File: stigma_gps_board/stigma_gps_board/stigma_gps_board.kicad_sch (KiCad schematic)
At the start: 7 parts, among them J2 Conn_02x05_Counter_Clockwise, U2 SAM-M10Q

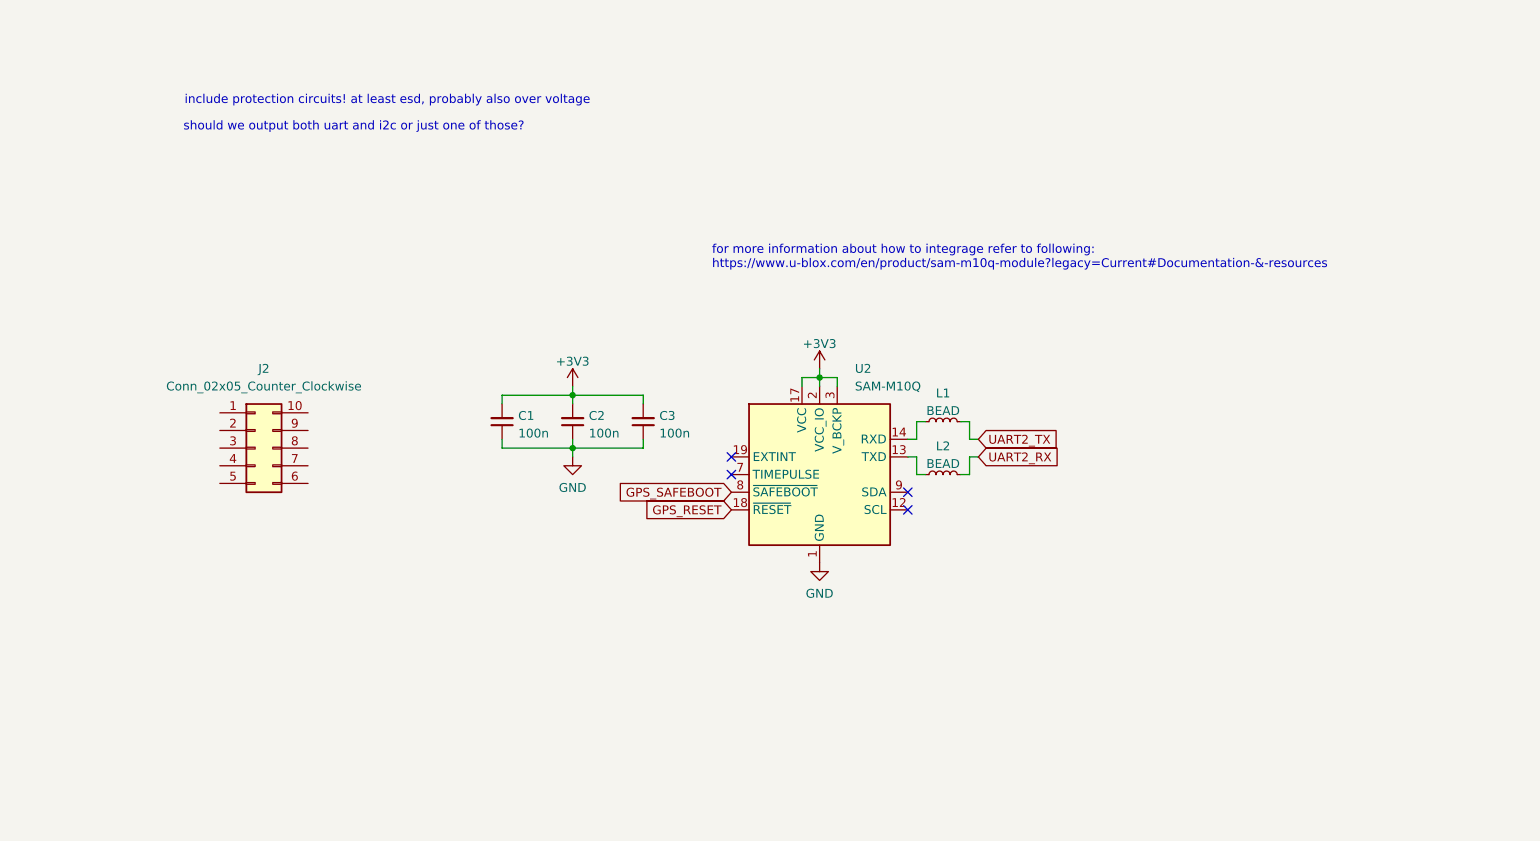
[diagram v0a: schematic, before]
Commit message: added esd protection, finished scematic
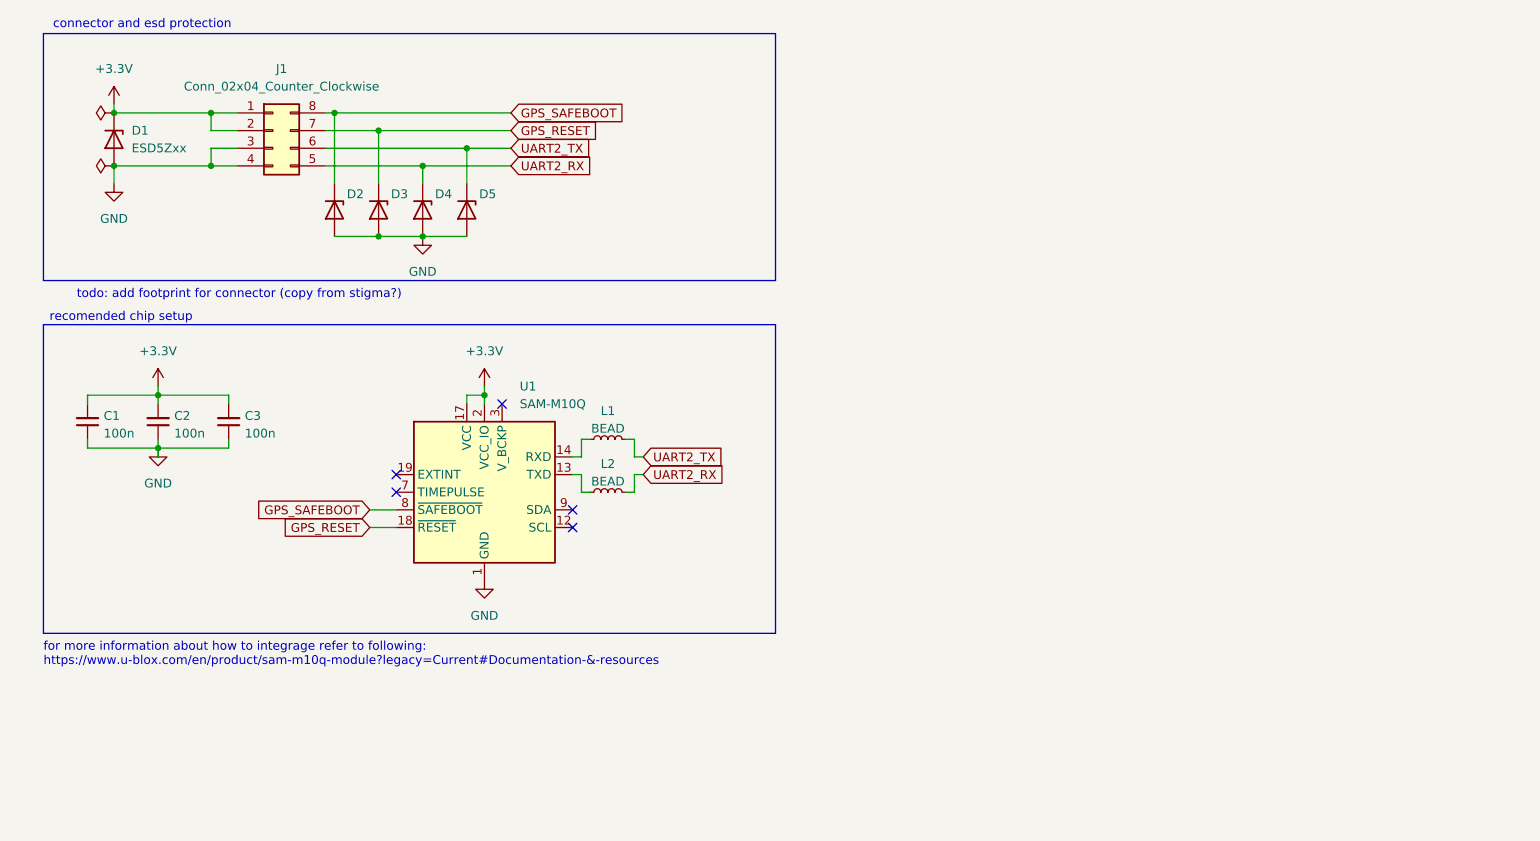
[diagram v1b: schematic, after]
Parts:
- removed J2: Conn_02x05_Counter_Clockwise, symbol Connector_Generic:Conn_02x05_Counter_Clockwise
- added D1, D2, D3, D4, D5: ESD5Zxx, Diode_SMD:D_SOD-523, symbol Diode:ESD5Zxx
- added J1: Conn_02x04_Counter_Clockwise, symbol Connector_Generic:Conn_02x04_Counter_Clockwise
- renumbered U2 to U1
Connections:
- net GND: now also D1.2 (A), D2.2 (A), D3.2 (A), D4.2 (A), D5.2 (A), J1.3 (Pin_3), J1.4 (Pin_4)
- net GPS_RESET: now also D3.1 (K), J1.7 (Pin_7)
- net GPS_SAFEBOOT: now also D2.1 (K), J1.8 (Pin_8)
- net UART2_RX: now also D4.1 (K), J1.5 (Pin_5)
- net UART2_TX: now also D5.1 (K), J1.6 (Pin_6)
- net +3V3 renamed +3.3V
- net +3.3V: now also D1.1 (K), J1.1 (Pin_1), J1.2 (Pin_2); no longer U1.3 (V_BCKP)
- no-connect marks 4 -> 5
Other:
- note added: "connector and esd protection"
- note added: "recomended chip setup"
- note added: "todo: add footprint for connector (copy from stigma?)"
- note removed: "include protection circuits! at least esd, probably also over voltage"
- note removed: "should we output both uart and i2c or just one of those?"
- moved on the sheet: C1, C2, C3, L1, L2, U1

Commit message: first revision of gps board finished
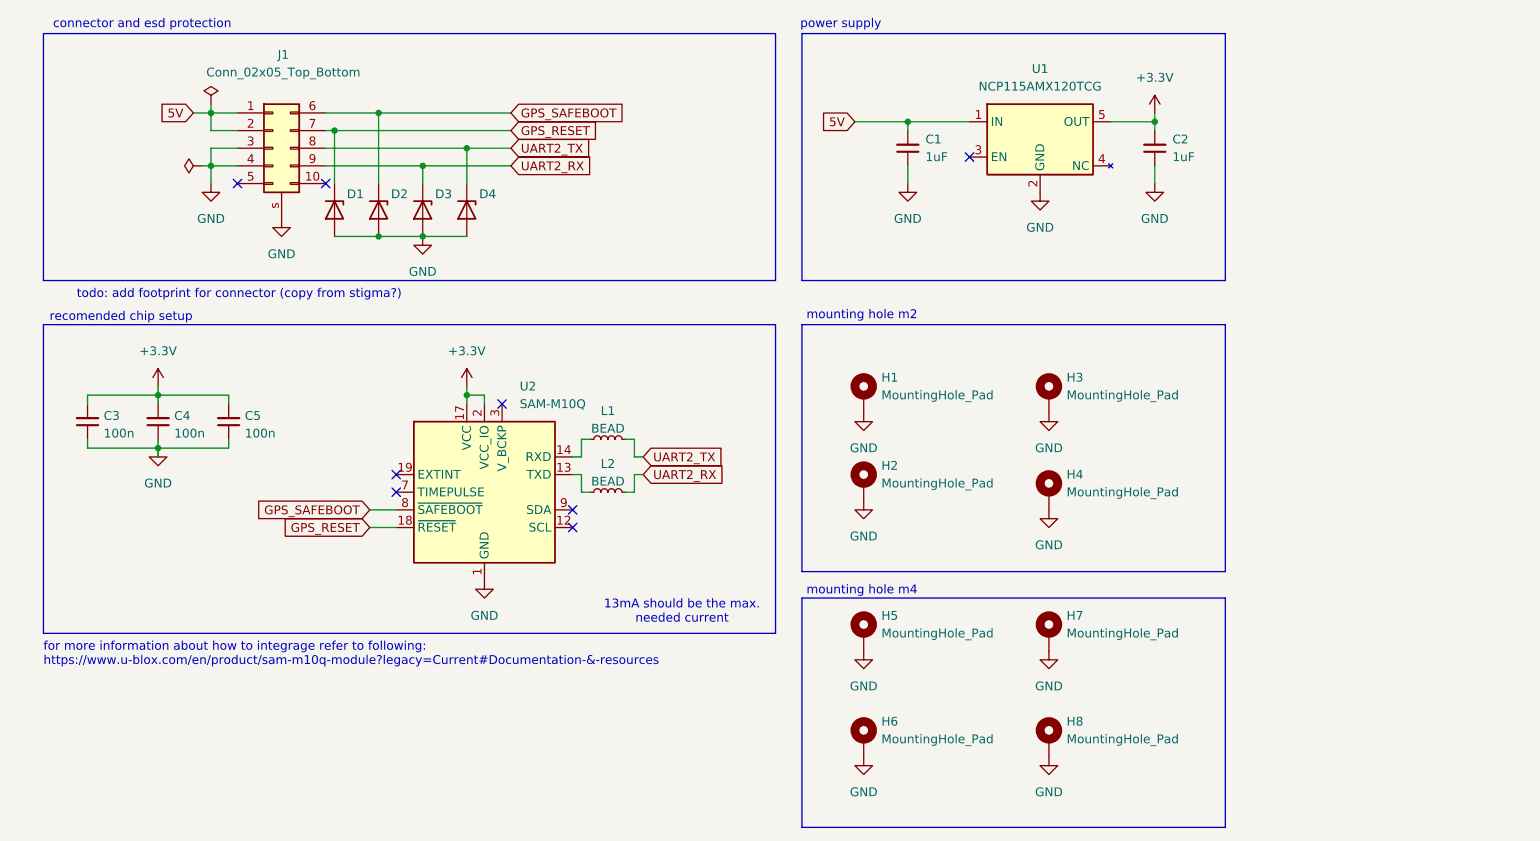
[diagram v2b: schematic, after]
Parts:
- removed D1: ESD5Zxx, Diode_SMD:D_SOD-523, symbol Diode:ESD5Zxx
- removed J1: Conn_02x04_Counter_Clockwise, symbol Connector_Generic:Conn_02x04_Counter_Clockwise
- added C1, C2: 1uF, Capacitor_SMD:C_0603_1608Metric_Pad1.08x0.95mm_HandSolder, symbol Device:C_Small
- added H1, H2, H3, H4: MountingHole_Pad, MountingHole:MountingHole_2.2mm_M2_DIN965_Pad_TopBottom, symbol Mechanical:MountingHole_Pad
- added H5, H6, H7, H8: MountingHole_Pad, MountingHole:MountingHole_4.3mm_M4_DIN965_Pad_TopBottom, symbol Mechanical:MountingHole_Pad
- added J1: Conn_02x05_Top_Bottom, stigma:DF40GB-10DP-0.4V-plug, symbol Connector_Generic:Conn_02x05_Top_Bottom
- added U1: NCP115AMX120TCG, Package_SO:TSOP-5_1.65x3.05mm_P0.95mm, symbol Regulator_Linear:NCP115AMX120TCG
- U2: renamed from U1; footprint RF_GPS:ublox_SAM-M8Q -> RF_GPS:ublox_SAM-M8Q_HandSolder
- renumbered C1 to C3, C2 to C4, C3 to C5, D2 to D1, D3 to D2, D4 to D3, D5 to D4
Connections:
- net +3.3V: now also C2.2, U1.5 (OUT)
- net GND: now also C1.1, C2.1, H1.1, H2.1, H3.1, H4.1, H5.1, H6.1, H7.1, H8.1, J1.3 (Pin_3), J1.4 (Pin_4), J1.s (shield), U1.2 (GND), U1.5 (OUT)
- net GPS_RESET: now also D1.1 (K), J1.7 (Pin_7); no longer D2.1 (K)
- net GPS_SAFEBOOT: now also D2.1 (K), J1.6 (Pin_6); no longer D1.1 (K)
- net UART2_RX: now also J1.9 (Pin_9)
- net UART2_TX: now also J1.8 (Pin_8)
- new net 5V: C1.2, J1.1 (Pin_1), J1.2 (Pin_2), U1.1 (IN)
- no-connect marks 5 -> 8
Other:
- note added: "13mA should be the max. needed current"
- note added: "mounting hole m2"
- note added: "mounting hole m4"
- note added: "power supply"
